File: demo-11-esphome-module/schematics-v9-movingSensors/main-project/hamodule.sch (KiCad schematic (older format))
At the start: 54 parts, among them J1 1017505, J2 Conn-ESP-Relays, J3 1017505, J4 Conn-Buttons, J5 Conn_01x02, J6 Conn-Esp-Sensors, J7 Conn-LedIndicators, J8 1017505, K1 G5Q-1, K2 G5Q-1, K3 G5Q-1, K4 G5Q-1, U1 ULN2003A, U2 LD1117S33TR_SOT223, U3 HCPL3700, U4 HCPL3700, U5 HCPL3700, U6 HCPL3700

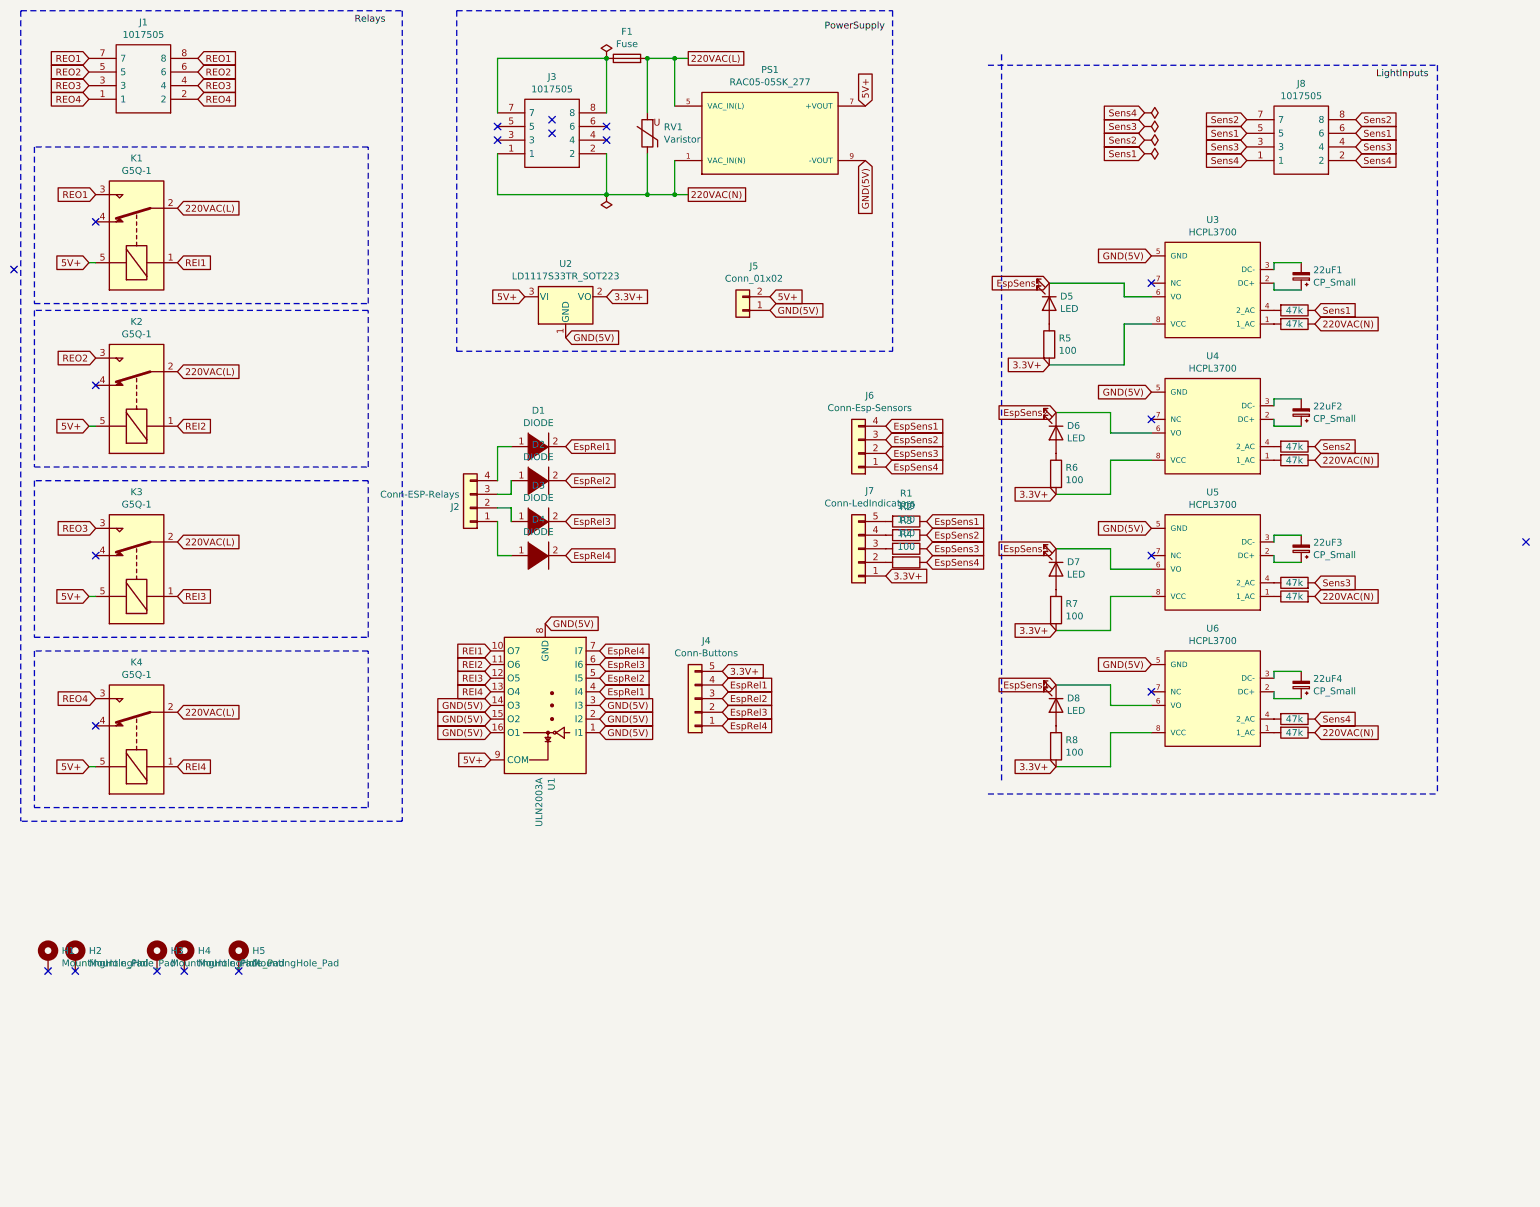
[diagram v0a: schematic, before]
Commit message: arranging 22v sensing
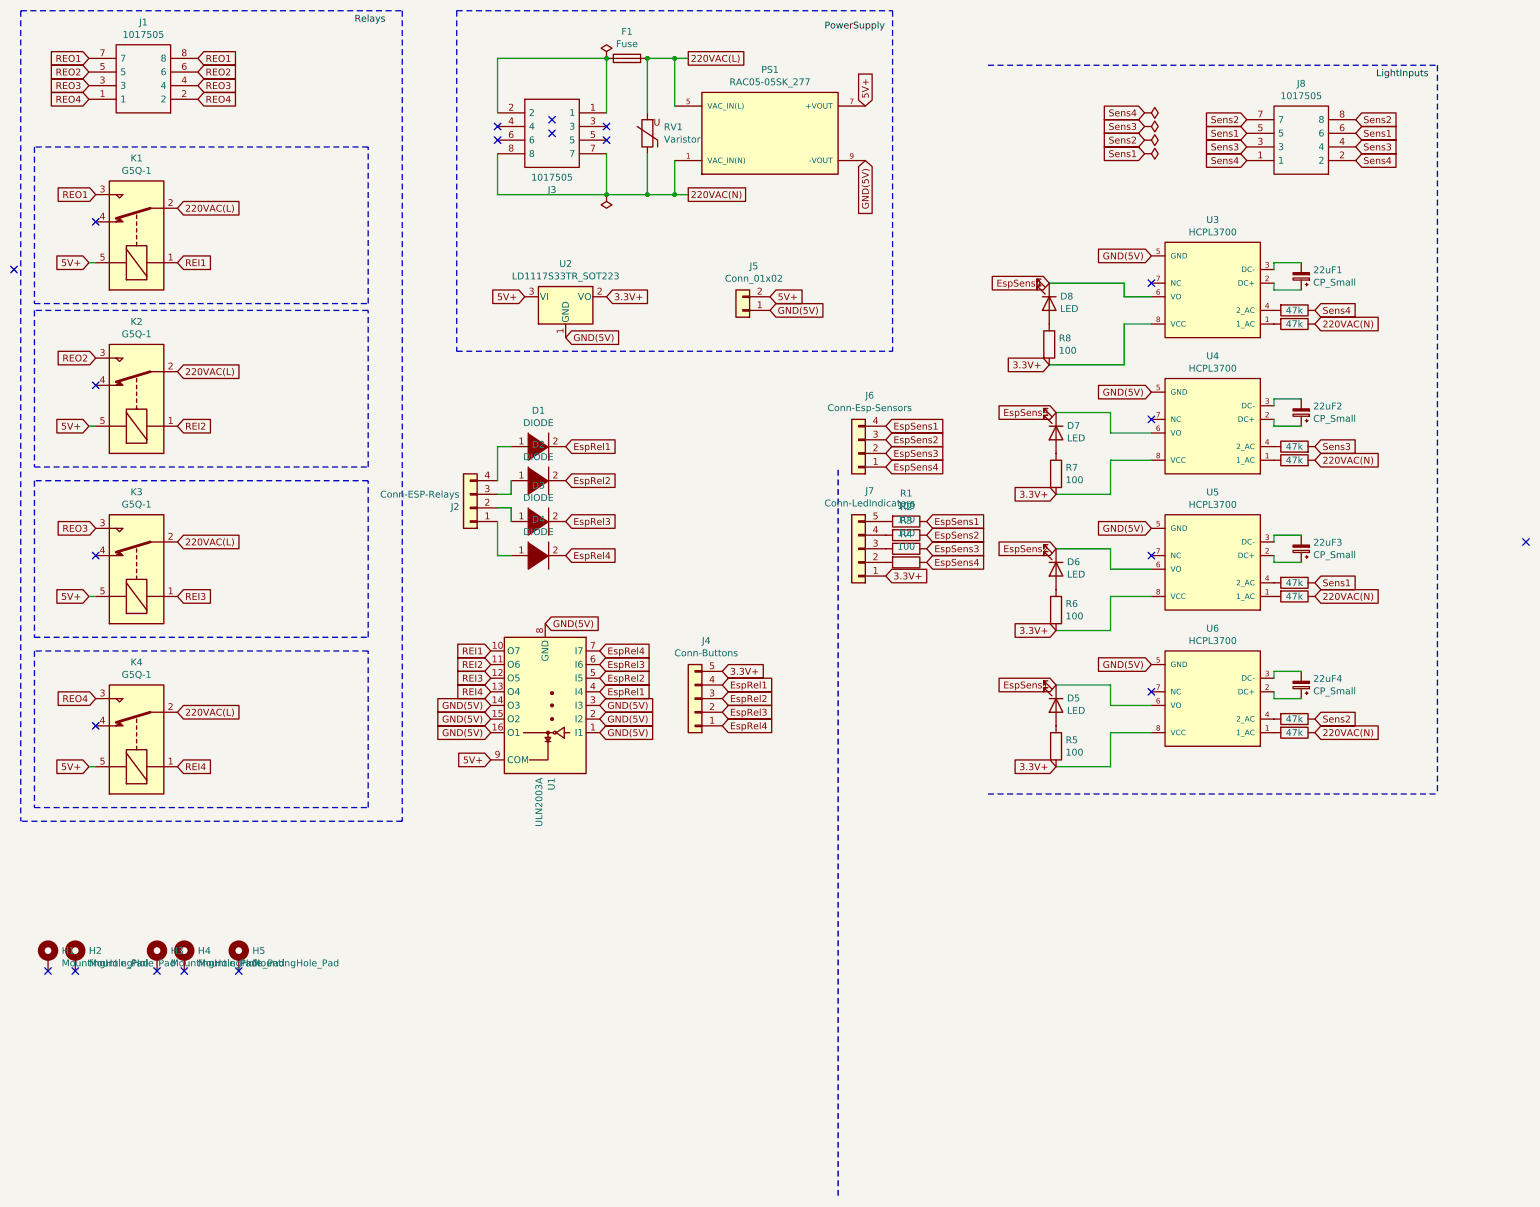
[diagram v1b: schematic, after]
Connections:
- net 220VAC(N): now also J3.7, J3.8; no longer J3.1, J3.2
- net EspSens1: now also U6.6 (VO); no longer U3.6 (VO)
- net EspSens2: now also U5.6 (VO); no longer U4.6 (VO)
- net EspSens3: now also U4.6 (VO); no longer U5.6 (VO)
- net EspSens4: now also U3.6 (VO); no longer U6.6 (VO)
- net at R9.2: now also U5.4 (2_AC); no longer U3.4 (2_AC)
- net at R10.2: now also U5.1 (1_AC); no longer U3.1 (1_AC)
- net at R12.2: now also U6.1 (1_AC); no longer U4.1 (1_AC)
- net at R11.2: now also U6.4 (2_AC); no longer U4.4 (2_AC)
- net at R13.1: now also U4.4 (2_AC); no longer U5.4 (2_AC)
- net at R14.1: now also U4.1 (1_AC); no longer U5.1 (1_AC)
- net at R16.2: now also U3.1 (1_AC); no longer U6.1 (1_AC)
- net at R15.2: now also U3.4 (2_AC); no longer U6.4 (2_AC)
- new net: F1.1, J3.1, J3.2
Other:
- moved on the sheet: D5, D6, D7, D8, R5, R6, R7, R8

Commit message: varistor + F.SilkS
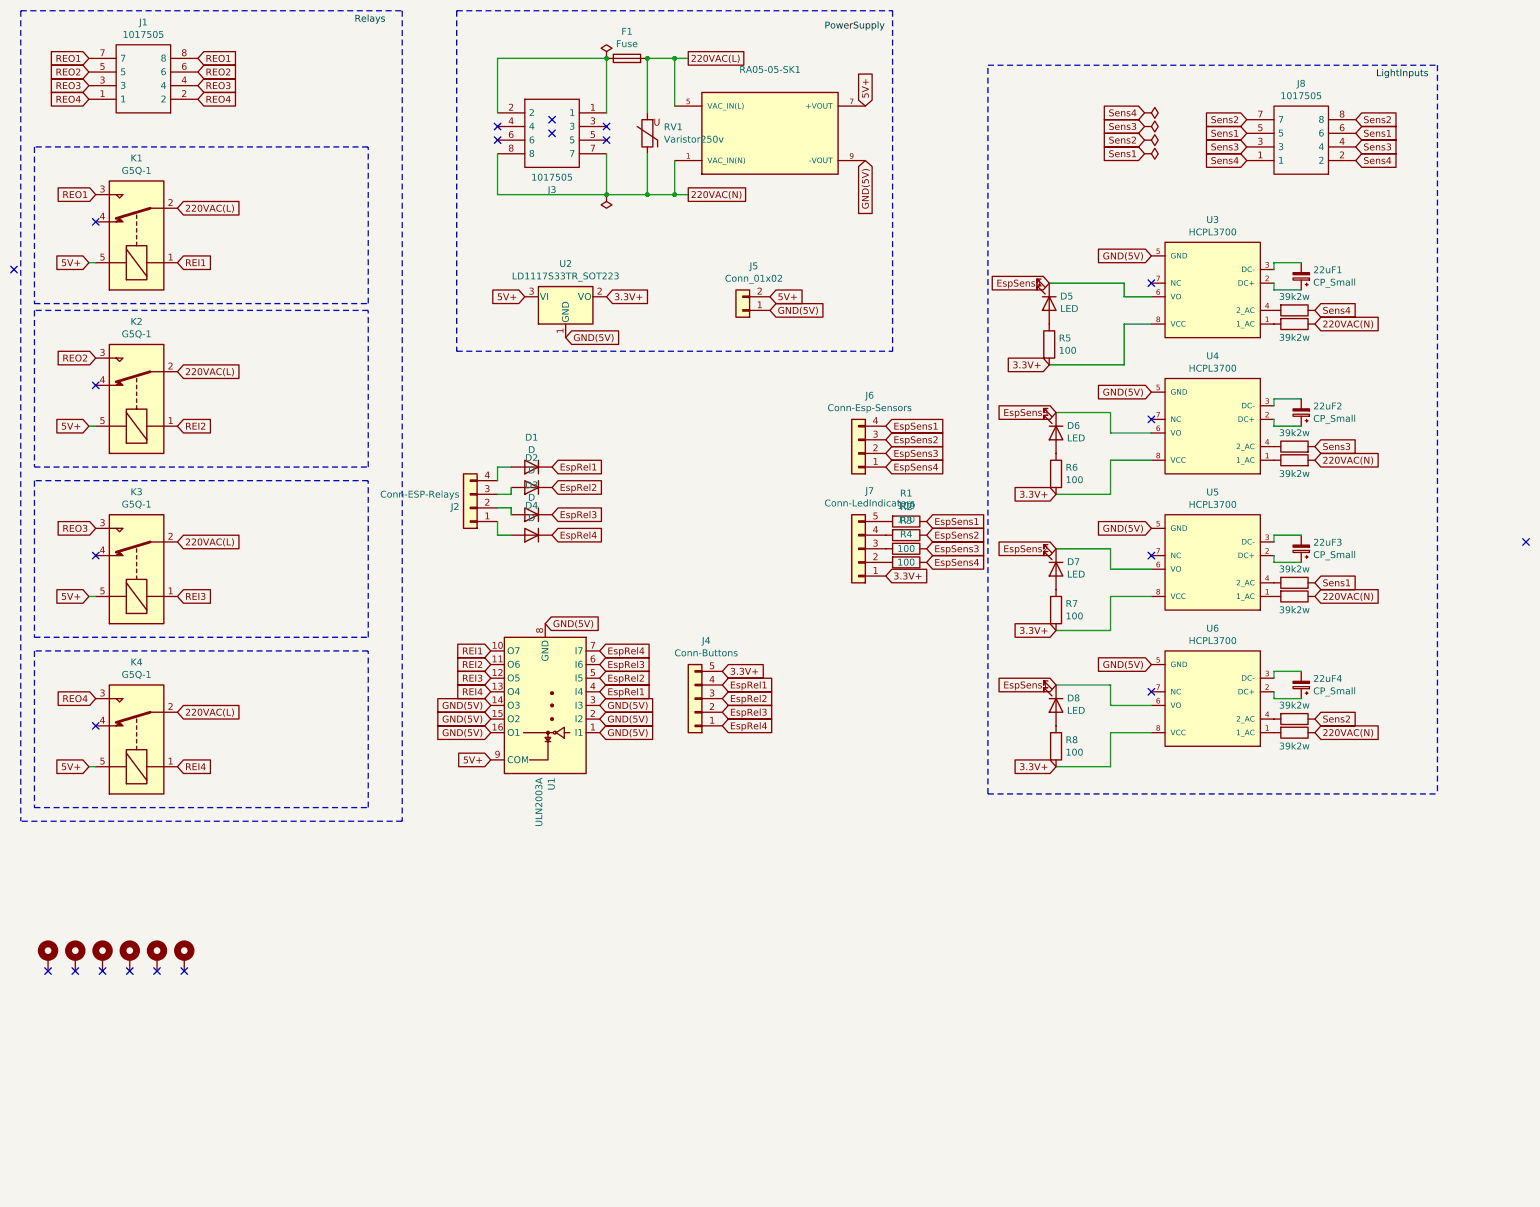
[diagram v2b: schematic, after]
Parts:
- removed D1, D2, D3, D4: DIODE, Diode_THT:D_DO-35_SOD27_P7.62mm_Horizontal, symbol pspice:DIODE
- added D1, D2, D3, D4: D, Diode_THT:D_A-405_P7.62mm_Horizontal, symbol Device:D
- added H3: MountingHole_Pad, MountingHole:MountingHole_3.2mm_M3_ISO14580_Pad, symbol Mechanical:MountingHole_Pad
- R10: renamed from R16; value 47k -> 39k2w
- R11: renamed from R13; value 47k -> 39k2w
- R12: renamed from R14; value 47k -> 39k2w
- R13: renamed from R9; value 47k -> 39k2w
- R14: renamed from R10; value 47k -> 39k2w
- R15: renamed from R11; value 47k -> 39k2w
- R16: renamed from R12; value 47k -> 39k2w
- R9: renamed from R15; value 47k -> 39k2w
- RV1: value Varistor -> Varistor250v; footprint Varistor:RV_Disc_D21.5mm_W5.3mm_P10mm -> Varistor:RV_Disc_D12mm_W4.2mm_P7.5mm
- renumbered D8 to D5, D7 to D6, D6 to D7, D5 to D8, H3 to H4, H4 to H5, H5 to H6, R8 to R5, R7 to R6, R6 to R7, R5 to R8, PS1 to RA05-05-SK1
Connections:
- net EspRel1: now also D1.1 (K)
- net EspRel2: now also D2.1 (K)
- net EspRel3: now also D3.1 (K)
- net EspRel4: now also D4.1 (K)
- net at J2.1 (Pin_1): now also D4.2 (A)
- net at J2.2 (Pin_2): now also D3.2 (A)
- net at J2.3 (Pin_3): now also D2.2 (A)
- net at J2.4 (Pin_4): now also D1.2 (A)
- no-connect marks 21 -> 22

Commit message: can't remember
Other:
- moved on the sheet: D1, D2, D3, D4, J2, J4, U1
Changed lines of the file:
@@
 Wire Wire Line
 	4100 1600 4100 1900
-Text GLabel 4450 5050 2    50   Input ~ 0
-GND(5V)
-Text GLabel 4850 5750 2    50   Input ~ 0
-GND(5V)
-Text GLabel 4850 5650 2    50   Input ~ 0
-GND(5V)
-Text GLabel 4850 5850 2    50   Input ~ 0
-GND(5V)
-Text GLabel 4050 5850 0    50   Input ~ 0
-GND(5V)
-Text GLabel 4050 5750 0    50   Input ~ 0
-GND(5V)
-Text GLabel 4050 5650 0    50   Input ~ 0
-GND(5V)
-Text GLabel 4050 5550 0    50   Input ~ 0
+Text GLabel 4350 4000 2    50   Input ~ 0
+GND(5V)
+Text GLabel 4750 4700 2    50   Input ~ 0
+GND(5V)
+Text GLabel 4750 4600 2    50   Input ~ 0
+GND(5V)
+Text GLabel 4750 4800 2    50   Input ~ 0
+GND(5V)
+Text GLabel 3950 4800 0    50   Input ~ 0
+GND(5V)
+Text GLabel 3950 4700 0    50   Input ~ 0
+GND(5V)
+Text GLabel 3950 4600 0    50   Input ~ 0
+GND(5V)
+Text GLabel 3950 4500 0    50   Input ~ 0
 REI4
-Text GLabel 4050 5450 0    50   Input ~ 0
+Text GLabel 3950 4400 0    50   Input ~ 0
 REI3
-Text GLabel 4050 5350 0    50   Input ~ 0
+Text GLabel 3950 4300 0    50   Input ~ 0
 REI2
-Text GLabel 4050 5250 0    50   Input ~ 0
+Text GLabel 3950 4200 0    50   Input ~ 0
 REI1
-Text GLabel 4050 6050 0    50   Input ~ 0
+Text GLabel 3950 5000 0    50   Input ~ 0
 5V+
 $Comp
 L Transistor_Array:ULN2003A U1
 U 1 1 61374AC1
-P 4450 5650
-F 0 "U1" V 4404 6180 50  0000 L CNN
-F 1 "ULN2003A" V 4495 6180 50  0000 L CNN
-F 2 "Package_DIP:DIP-16_W7.62mm_LongPads" H 4500 5100 50  0001 L CNN
-F 3 "http://www.ti.com/lit/ds/symlink/uln2003a.pdf" H 4550 5450 50  0001 C CNN
-	1    4450 5650
+P 4350 4600
+F 0 "U1" V 4304 5130 50  0000 L CNN
+F 1 "ULN2003A" V 4395 5130 50  0000 L CNN
+F 2 "Package_DIP:DIP-16_W7.62mm_LongPads" H 4400 4050 50  0001 L CNN
+F 3 "http://www.ti.com/lit/ds/symlink/uln2003a.pdf" H 4450 4400 50  0001 C CNN
+	1    4350 4600
 	-1   0    0    1
 $EndComp
@@
 L Connector_Generic:Conn_01x05 J4
 U 1 1 61516260
-P 5550 5600
-F 0 "J4" H 5468 5175 50  0000 C CNN
-F 1 "Conn-Buttons" H 5468 5266 50  0000 C CNN
-F 2 "Connector_JST:JST_XH_B5B-XH-A_1x05_P2.50mm_Vertical" H 5550 5600 50  0001 C CNN
-F 3 "~" H 5550 5600 50  0001 C CNN
-	1    5550 5600
-	-1   0    0    1
-$EndComp
-Text GLabel 5750 5500 2    50   Input ~ 0
+P 5450 4550
+F 0 "J4" H 5368 4125 50  0000 C CNN
+F 1 "Conn-Buttons" H 5368 4216 50  0000 C CNN
+F 2 "Connector_JST:JST_XH_B5B-XH-A_1x05_P2.50mm_Vertical" H 5450 4550 50  0001 C CNN
+F 3 "~" H 5450 4550 50  0001 C CNN
+	1    5450 4550
+	-1   0    0    1
+$EndComp
+Text GLabel 5650 4450 2    50   Input ~ 0
 EspRel1
-Text GLabel 5750 5600 2    50   Input ~ 0
+Text GLabel 5650 4550 2    50   Input ~ 0
 EspRel2
-Text GLabel 5750 5700 2    50   Input ~ 0
+Text GLabel 5650 4650 2    50   Input ~ 0
 EspRel3
-Text GLabel 5750 5800 2    50   Input ~ 0
+Text GLabel 5650 4750 2    50   Input ~ 0
 EspRel4
 Text GLabel 8200 4500 0    50   Input ~ 0
@@
 Text GLabel 1100 2400 0    50   Input ~ 0
 5V+
-Text GLabel 4500 3900 2    50   Input ~ 0
+Text GLabel 4450 3300 2    50   Input ~ 0
 EspRel1
-Text GLabel 4500 4050 2    50   Input ~ 0
+Text GLabel 4450 3450 2    50   Input ~ 0
 EspRel2
-Text GLabel 4500 4250 2    50   Input ~ 0
+Text GLabel 4450 3650 2    50   Input ~ 0
 EspRel3
-Text GLabel 4500 4400 2    50   Input ~ 0
+Text GLabel 4450 3800 2    50   Input ~ 0
 EspRel4
-Text GLabel 4850 5550 2    50   Input ~ 0
+Text GLabel 4750 4500 2    50   Input ~ 0
 EspRel1
-Text GLabel 4850 5450 2    50   Input ~ 0
+Text GLabel 4750 4400 2    50   Input ~ 0
 EspRel2
-Text GLabel 4850 5350 2    50   Input ~ 0
+Text GLabel 4750 4300 2    50   Input ~ 0
 EspRel3
-Text GLabel 4850 5250 2    50   Input ~ 0
+Text GLabel 4750 4200 2    50   Input ~ 0
 EspRel4
-Text GLabel 5750 5400 2    50   Input ~ 0
-3.3V+
-Wire Wire Line
-	4200 4100 4100 4100
-Wire Wire Line
-	4100 4200 4200 4200
+Text GLabel 5650 4350 2    50   Input ~ 0
+3.3V+
+Wire Wire Line
+	4150 3500 4050 3500
+Wire Wire Line
+	4050 3600 4150 3600
 Text GLabel 9600 1650 0    50   Input ~ 0
 Sens4
@@
 L Connector_Generic:Conn_01x04 J2
 U 1 1 614144AF
-P 3900 4200
-F 0 "J2" H 3980 4192 50  0000 L CNN
-F 1 "Conn-ESP-Relays" H 3980 4101 50  0000 L CNN
-F 2 "Connector_JST:JST_XH_B4B-XH-A_1x04_P2.50mm_Vertical" H 3900 4200 50  0001 C CNN
-F 3 "~" H 3900 4200 50  0001 C CNN
-	1    3900 4200
+P 3850 3600
+F 0 "J2" H 3930 3592 50  0000 L CNN
+F 1 "Conn-ESP-Relays" H 3930 3501 50  0000 L CNN
+F 2 "Connector_JST:JST_XH_B4B-XH-A_1x04_P2.50mm_Vertical" H 3850 3600 50  0001 C CNN
+F 3 "~" H 3850 3600 50  0001 C CNN
+	1    3850 3600
 	-1   0    0    1
 $EndComp
@@
 L Device:D D1
 U 1 1 615714B6
-P 4350 3900
-F 0 "D1" H 4350 3683 50  0000 C CNN
-F 1 "D" H 4350 3774 50  0000 C CNN
-F 2 "Diode_THT:D_A-405_P7.62mm_Horizontal" H 4350 3900 50  0001 C CNN
-F 3 "~" H 4350 3900 50  0001 C CNN
-	1    4350 3900
+P 4300 3300
+F 0 "D1" H 4300 3083 50  0000 C CNN
+F 1 "D" H 4300 3174 50  0000 C CNN
+F 2 "Diode_THT:D_A-405_P7.62mm_Horizontal" H 4300 3300 50  0001 C CNN
+F 3 "~" H 4300 3300 50  0001 C CNN
+	1    4300 3300
 	-1   0    0    1
 $EndComp
@@
 L Device:D D2
 U 1 1 615764D6
-P 4350 4050
-F 0 "D2" H 4350 3833 50  0000 C CNN
-F 1 "D" H 4350 3924 50  0000 C CNN
-F 2 "Diode_THT:D_A-405_P7.62mm_Horizontal" H 4350 4050 50  0001 C CNN
-F 3 "~" H 4350 4050 50  0001 C CNN
-	1    4350 4050
+P 4300 3450
+F 0 "D2" H 4300 3233 50  0000 C CNN
+F 1 "D" H 4300 3324 50  0000 C CNN
+F 2 "Diode_THT:D_A-405_P7.62mm_Horizontal" H 4300 3450 50  0001 C CNN
+F 3 "~" H 4300 3450 50  0001 C CNN
+	1    4300 3450
 	-1   0    0    1
 $EndComp
@@
 L Device:D D3
 U 1 1 615780DE
-P 4350 4250
-F 0 "D3" H 4350 4033 50  0000 C CNN
-F 1 "D" H 4350 4124 50  0000 C CNN
-F 2 "Diode_THT:D_A-405_P7.62mm_Horizontal" H 4350 4250 50  0001 C CNN
-F 3 "~" H 4350 4250 50  0001 C CNN
-	1    4350 4250
+P 4300 3650
+F 0 "D3" H 4300 3433 50  0000 C CNN
+F 1 "D" H 4300 3524 50  0000 C CNN
+F 2 "Diode_THT:D_A-405_P7.62mm_Horizontal" H 4300 3650 50  0001 C CNN
+F 3 "~" H 4300 3650 50  0001 C CNN
+	1    4300 3650
 	-1   0    0    1
 $EndComp
@@
 L Device:D D4
 U 1 1 6157A0C6
-P 4350 4400
-F 0 "D4" H 4350 4183 50  0000 C CNN
-F 1 "D" H 4350 4274 50  0000 C CNN
-F 2 "Diode_THT:D_A-405_P7.62mm_Horizontal" H 4350 4400 50  0001 C CNN
-F 3 "~" H 4350 4400 50  0001 C CNN
-	1    4350 4400
-	-1   0    0    1
-$EndComp
-Wire Wire Line
-	4200 3900 4100 3900
-Wire Wire Line
-	4100 3900 4100 4000
-Wire Wire Line
-	4200 4400 4100 4400
-Wire Wire Line
-	4100 4400 4100 4300
-Wire Wire Line
-	4200 4250 4200 4200
-Wire Wire Line
-	4200 4050 4200 4100
+P 4300 3800
+F 0 "D4" H 4300 3583 50  0000 C CNN
+F 1 "D" H 4300 3674 50  0000 C CNN
+F 2 "Diode_THT:D_A-405_P7.62mm_Horizontal" H 4300 3800 50  0001 C CNN
+F 3 "~" H 4300 3800 50  0001 C CNN
+	1    4300 3800
+	-1   0    0    1
+$EndComp
+Wire Wire Line
+	4150 3300 4050 3300
+Wire Wire Line
+	4050 3300 4050 3400
+Wire Wire Line
+	4150 3800 4050 3800
+Wire Wire Line
+	4050 3800 4050 3700
+Wire Wire Line
+	4150 3650 4150 3600
+Wire Wire Line
+	4150 3450 4150 3500
 $EndSCHEMATC
